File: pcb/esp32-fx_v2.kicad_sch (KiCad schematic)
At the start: 79 parts, among them J1 AudioJack2 (out), J2 AudioJack2 (in), K1 G6E-134P-US-DC3, P1 USB_C_Plug_USB2.0, Q1 MMBT2222A, SW1 SW_Push, U1 ESP32-S3-WROOM-1, U10 OPA1655DBV, U11 D3V3XA4B10LP, U2 TPD1E05U06DYA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

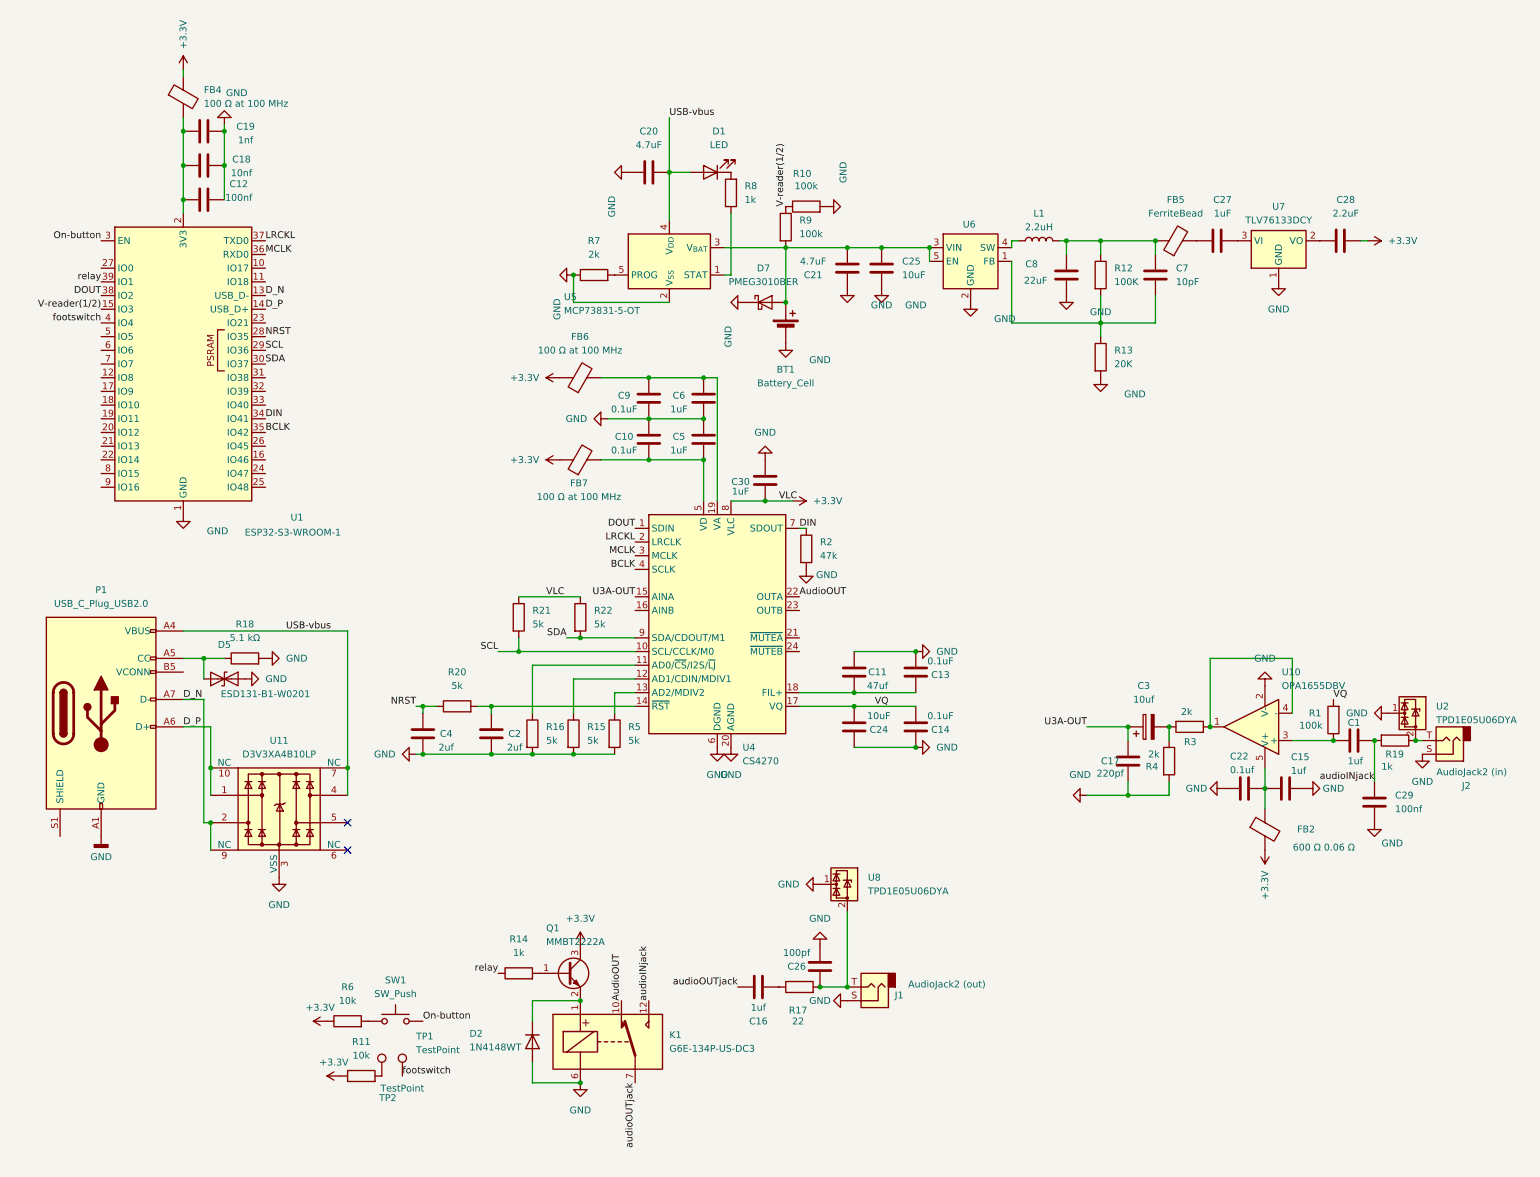
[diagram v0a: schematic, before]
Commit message: fixed input and output values and removed opamp
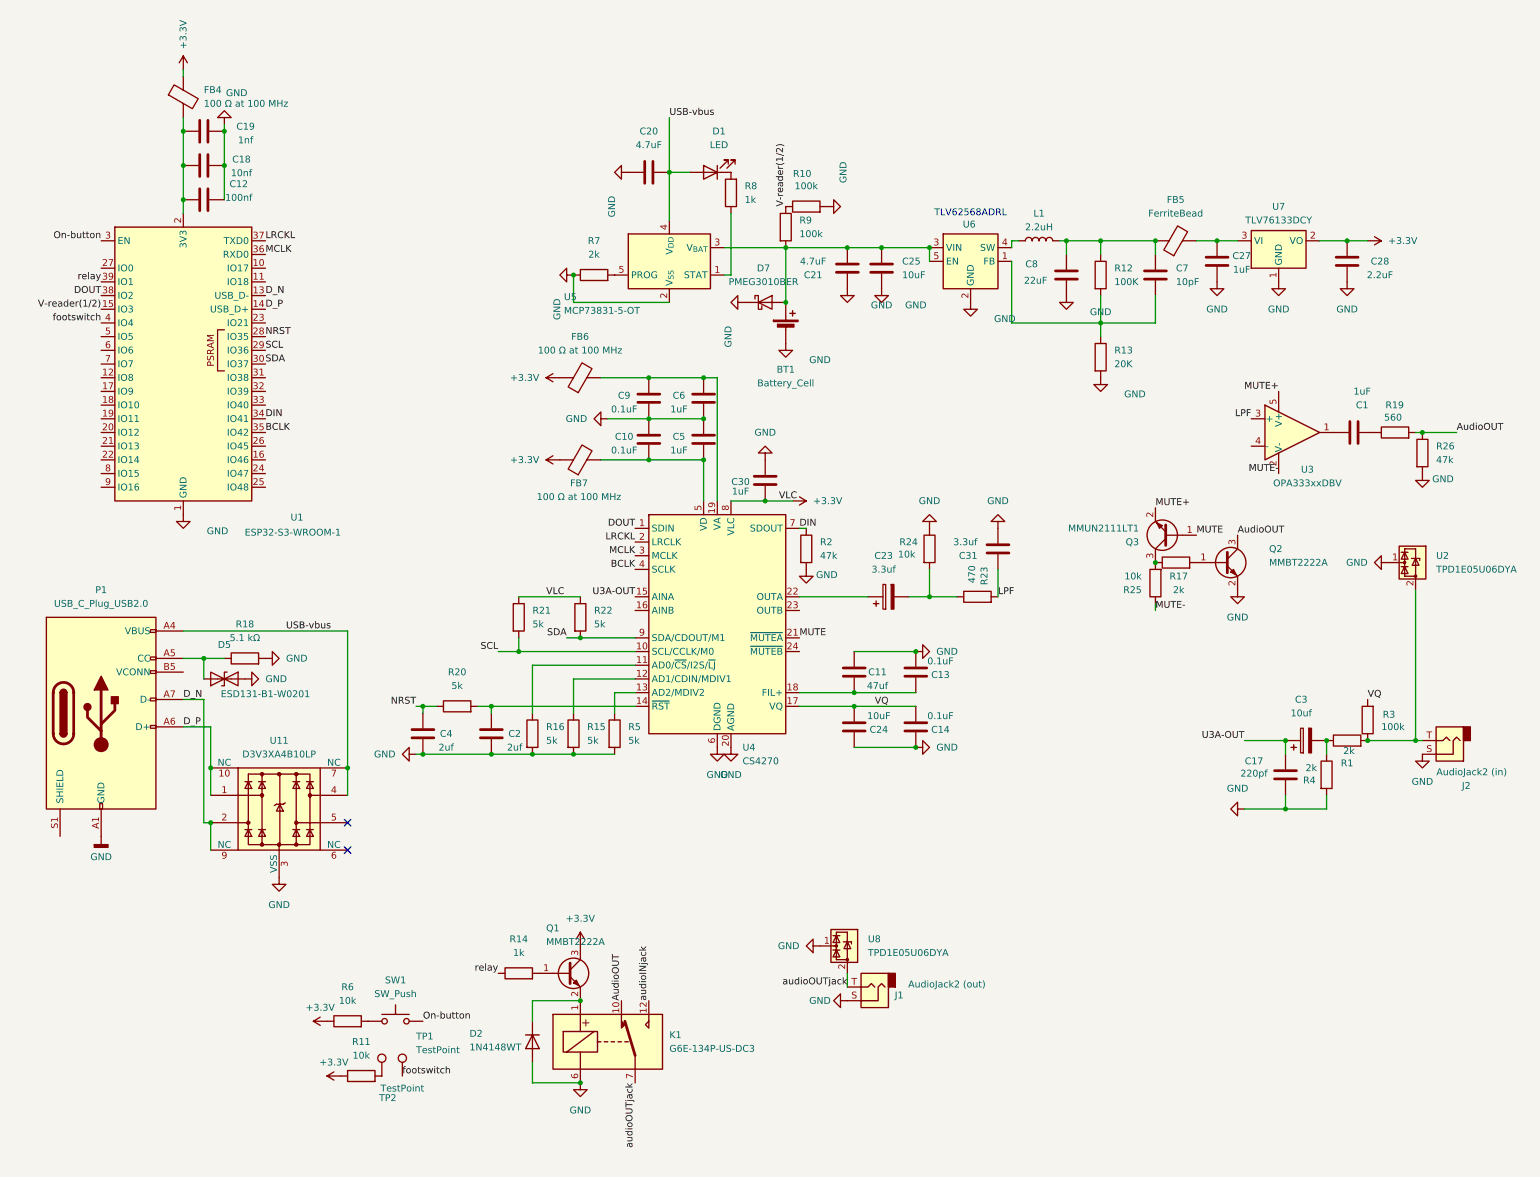
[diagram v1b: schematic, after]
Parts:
- removed C15, C16: 1uf, Capacitor_SMD:C_0603_1608Metric, symbol Device:C
- removed C22: 0.1uf, Capacitor_SMD:C_0603_1608Metric, symbol Device:C
- removed C26: 100pf, Capacitor_SMD:C_0603_1608Metric, symbol Device:C
- removed C29: 100nf, Capacitor_SMD:C_0603_1608Metric, symbol Device:C
- removed FB2: 600 Ω 0.06 Ω, Inductor_SMD:L_0603_1608Metric, symbol Device:FerriteBead
- removed U10: OPA1655DBV, Package_TO_SOT_SMD:SOT-23-5, symbol Amplifier_Operational:OPA1655DBV
- added C23: 3.3uf, Capacitor_SMD:C_0805_2012Metric, symbol Device:C_Polarized
- added C31: 3.3uf, Capacitor_SMD:C_0805_2012Metric, symbol Device:C
- added Q2: MMBT2222A, Package_TO_SOT_SMD:SOT-23, symbol Transistor_BJT:MMBT2222A
- added Q3: MMUN2111LT1, Package_TO_SOT_SMD:SOT-23, symbol Transistor_BJT:MMBT2222A
- added R23: 470, Resistor_SMD:R_0603_1608Metric, symbol Device:R
- added R24, R25: 10k, Resistor_SMD:R_0603_1608Metric, symbol Device:R
- added R26: 47k, Resistor_SMD:R_0603_1608Metric, symbol Device:R
- added U3: OPA333xxDBV, Package_TO_SOT_SMD:SOT-23-5, symbol Amplifier_Operational:OPA333xxDBV
- C1: value 1uf -> 1uF; footprint Capacitor_SMD:C_0603_1608Metric -> Capacitor_SMD:C_0805_2012Metric
- C11, C17, C2, C4: footprint Capacitor_SMD:C_0603_1608Metric -> Capacitor_SMD:C_0805_2012Metric
- C3: footprint Capacitor_SMD:C_1210_3225Metric -> Capacitor_SMD:C_0805_2012Metric
- R1: value 100k -> 2k
- R17: value 22 -> 2k
- R19: value 1k -> 560
- R3: value 2k -> 100k
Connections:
- net +3.3V: now also C28.1, U7.2 (VO); no longer C28.2
- net AudioOUT: now also R19.2, Q2.3 (C), R26.1; no longer U4.22 (OUTA)
- net GND: now also C27.1, C28.2, C31.1, Q2.2 (E), R24.1, R26.2
- net VQ: now also R3.2; no longer R1.2
- net audioINjack: no longer C1.2, R19.2
- net audioOUTjack: now also J1.T, U8.2 (GND)
- net at C1.1: now also U3.1; no longer R1.1
- net at C3.2, R4.1: now also R1.1; no longer R3.2
- net at R3.1: now also J2.T, R1.2, U2.2 (GND)
- net at FB5.2: now also C27.2, U7.3 (VI); no longer C27.1
- net MUTE: now reaches U4.21 (~{MUTEA})
- net MUTE: now also Q3.1 (B)
- net at R17.1: now also Q3.3 (C), R25.2
- new net: C23.2, R23.1, R24.2
- new net: Q2.1 (B), R17.2
- new net: C1.2, R19.1
- new net: C23.1, U4.22 (OUTA)
- new net LPF: C31.2, R23.2, U3.3 (+)
- new net MUTE+: Q3.2 (E), U3.5 (V+)
- new net MUTE-: R25.1, U3.2 (V-)
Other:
- note added: "TLV62568ADRL"
- moved on the sheet: C17, C27, C28, C3, R4, U2, U8

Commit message: added mute layout
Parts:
- C11: value 47uf -> 10uf; footprint Capacitor_SMD:C_0805_2012Metric -> Capacitor_SMD:C_0603_1608Metric
- C13, C14: footprint Capacitor_SMD:C_0805_2012Metric -> Capacitor_SMD:C_0603_1608Metric
- C24: value 10uF -> 47uF; footprint Capacitor_SMD:C_0805_2012Metric -> Capacitor_SMD:C_0603_1608Metric
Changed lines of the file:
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@@
 			)
 		)
-		(property "Value" "47uf"
+		(property "Value" "10uf"
 			(at 173.228 111.76 0)
 			(effects
@@
 			)
 		)
-		(property "Footprint" "Capacitor_SMD:C_0805_2012Metric"
+		(property "Footprint" "Capacitor_SMD:C_0603_1608Metric"
 			(at 167.9448 105.41 0)
 			(effects
@@
 			)
 		)
-		(property "Value" "10uF"
+		(property "Value" "47uF"
 			(at 173.482 117.348 0)
 			(effects
@@
 			)
 		)
-		(property "Footprint" "Capacitor_SMD:C_0805_2012Metric"
+		(property "Footprint" "Capacitor_SMD:C_0603_1608Metric"
 			(at 169.8752 123.19 0)
 			(effects
@@
 			)
 		)
-		(property "Footprint" "Capacitor_SMD:C_0805_2012Metric"
+		(property "Footprint" "Capacitor_SMD:C_0603_1608Metric"
 			(at 181.3052 123.19 0)
 			(effects
@@
 			)
 		)
-		(property "Footprint" "Capacitor_SMD:C_0805_2012Metric"
+		(property "Footprint" "Capacitor_SMD:C_0603_1608Metric"
 			(at 181.3052 113.03 0)
 			(effects

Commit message: added back opamp
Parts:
- removed R3: 100k, Resistor_SMD:R_0603_1608Metric, symbol Device:R
- added C15: 0.1uF, Capacitor_SMD:C_0805_2012Metric, symbol Device:C
- added C16: 1uF, Capacitor_SMD:C_0805_2012Metric, symbol Device:C
- added FB1: 100 Ω at 100 MHz, Inductor_SMD:L_0805_2012Metric, symbol Device:FerriteBead
- added U9: OPA333xxDBV, Package_TO_SOT_SMD:SOT-23-5, symbol Amplifier_Operational:OPA333xxDBV
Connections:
- net +3.3V: now also FB1.1
- net GND: now also C15.2, C16.2, U9.2 (V-)
- net U3A-OUT: now also U9.1, U9.4 (-); no longer C17.2, C3.1
- net VQ: no longer names the net of C14.1, C24.1, U4.17 (VQ)
- new net: C17.2, C3.1, U9.3 (+)
- new net: C15.1, C16.1, FB1.2, U9.5 (V+)
